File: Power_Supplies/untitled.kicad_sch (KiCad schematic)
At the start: 6 parts, among them U6 CS4391A-KZZ

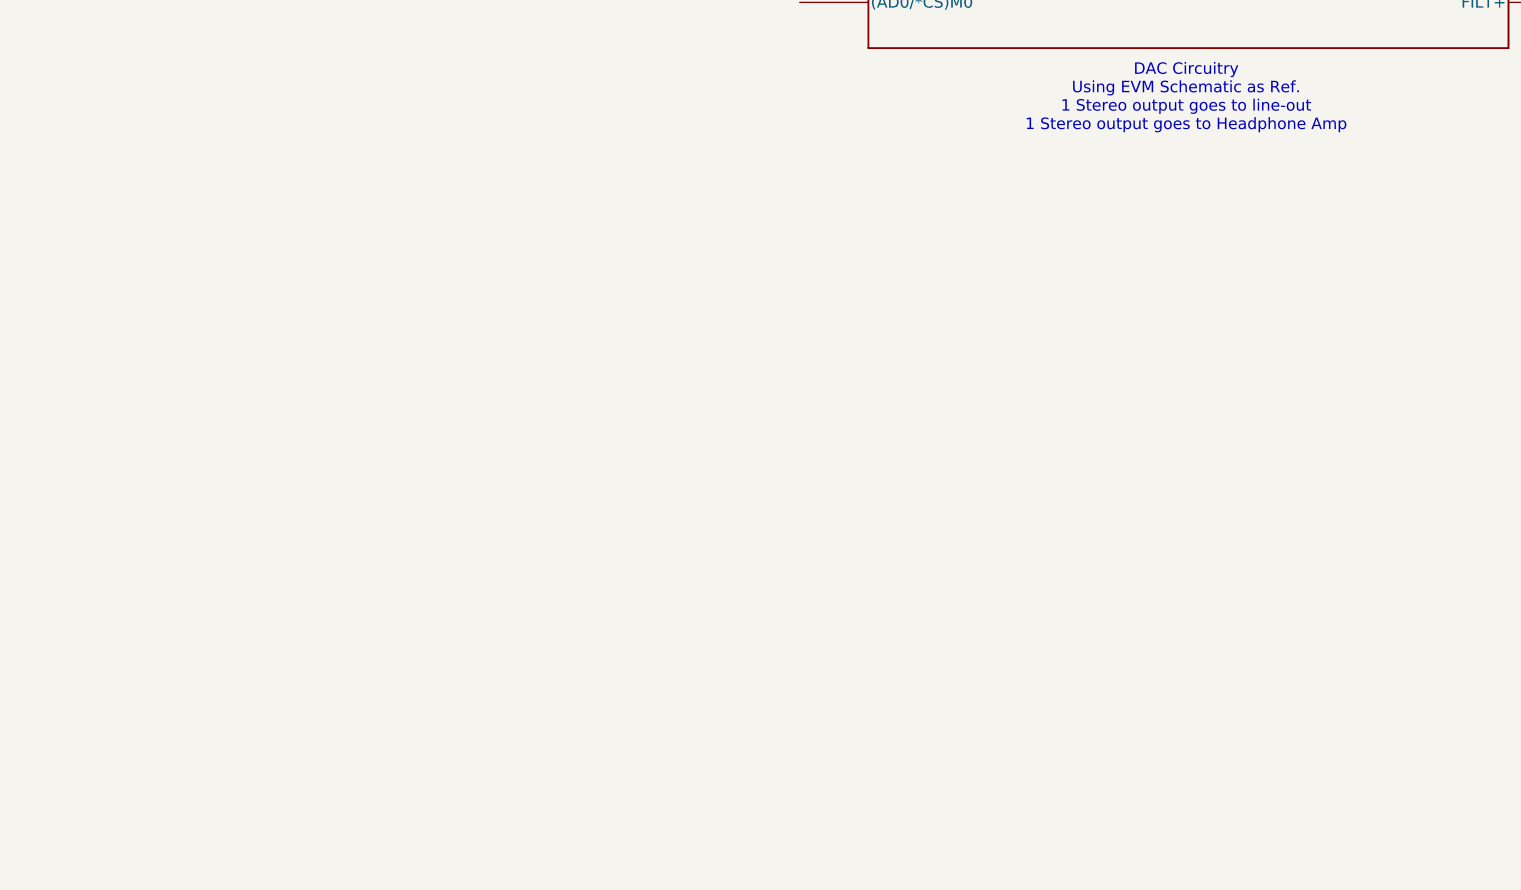
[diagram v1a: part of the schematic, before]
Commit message: Added Phantom Power, updated Xcore library things
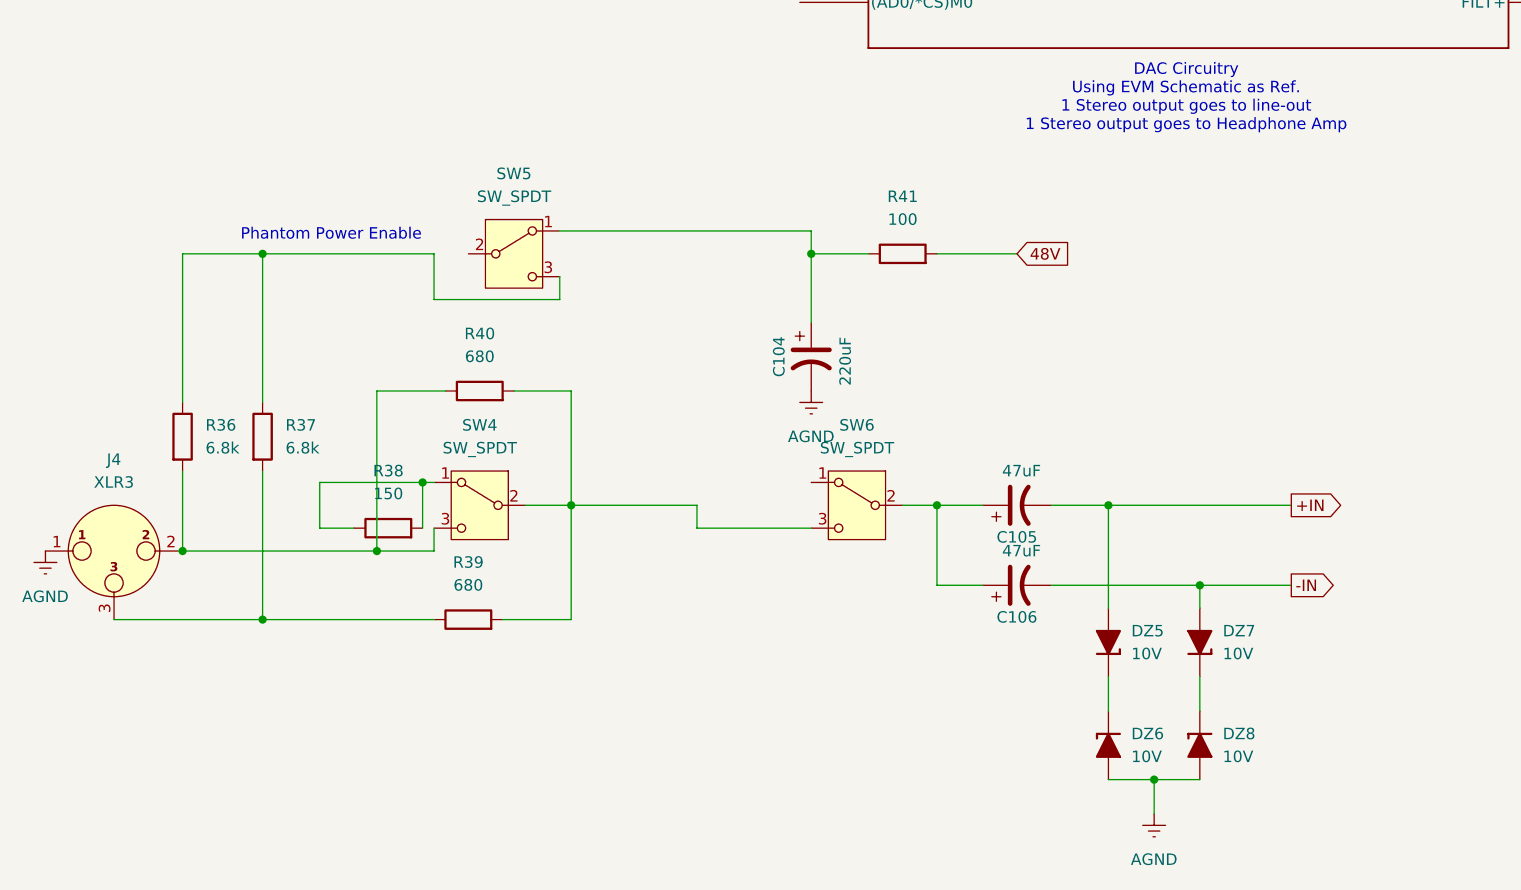
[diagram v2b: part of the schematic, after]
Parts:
- added C104: 220uF, Capacitor_SMD:CP_Elec_4x5.8, symbol Device:C_Polarized_US
- added C105, C106: 47uF, Capacitor_SMD:CP_Elec_4x5.8, symbol Device:C_Polarized_US
- added DZ5, DZ6, DZ7, DZ8: 10V, Diode_SMD:D_SMB, symbol PCM_Diode_Zener_AKL:D_Zener_Generic
- added J4: XLR3, symbol Connector_Audio:XLR3
- added R36, R37: 6.8k, Resistor_SMD:R_0805_2012Metric, symbol Device:R
- added R38: 150, Resistor_SMD:R_0805_2012Metric, symbol Device:R
- added R39, R40: 680, Resistor_SMD:R_0805_2012Metric, symbol Device:R
- added R41: 100, Resistor_SMD:R_0805_2012Metric, symbol Device:R
- added SW4, SW5, SW6: SW_SPDT, symbol Switch:SW_SPDT
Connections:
- net AGND: now also C104.2, DZ6.2 (A), DZ8.2 (A), J4.1
- new net: R38.1, R38.2, SW4.1 (A)
- new net: DZ5.1 (K), DZ6.1 (K)
- new net: C104.1, R41.1, SW5.1 (A)
- new net: R36.1, R37.1, SW5.3 (C)
- new net: J4.2, R36.2, R40.1, SW4.3 (C)
- new net: R39.2, R40.2, SW4.2 (B), SW6.3 (C)
- new net: DZ7.1 (K), DZ8.1 (K)
- new net: C105.1, C106.1, SW6.2 (B)
- new net: J4.3, R37.2, R39.1
- new net +IN: C105.2, DZ5.2 (A)
- new net -IN: C106.2, DZ7.2 (A)
- new net 48V: R41.2
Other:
- note added: "Phantom Power Enable"

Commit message: Add files via upload
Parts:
- C104, C105, C106, C14, C15, C16, C17, C18, DZ5, DZ6, DZ7, DZ8, J4, R36, R37, R38, R39, R40, R41, SW4, SW5, SW6, U6: now left out of the parts list
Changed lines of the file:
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@@
 		(unit 1)
 		(exclude_from_sim no)
-		(in_bom yes)
-		(on_board yes)
+		(in_bom no)
+		(on_board no)
 		(dnp no)
 		(fields_autoplaced yes)
@@
 		(unit 1)
 		(exclude_from_sim no)
-		(in_bom yes)
-		(on_board yes)
+		(in_bom no)
+		(on_board no)
 		(dnp no)
 		(fields_autoplaced yes)
@@
 		(unit 1)
 		(exclude_from_sim no)
-		(in_bom yes)
-		(on_board yes)
+		(in_bom no)
+		(on_board no)
 		(dnp no)
 		(fields_autoplaced yes)
@@
 		(unit 1)
 		(exclude_from_sim no)
-		(in_bom yes)
-		(on_board yes)
+		(in_bom no)
+		(on_board no)
 		(dnp no)
 		(property "Reference" "C104"
@@
 		(unit 1)
 		(exclude_from_sim no)
-		(in_bom yes)
-		(on_board yes)
+		(in_bom no)
+		(on_board no)
 		(dnp no)
 		(fields_autoplaced yes)
@@
 		(unit 1)
 		(exclude_from_sim no)
-		(in_bom yes)
-		(on_board yes)
+		(in_bom no)
+		(on_board no)
 		(dnp no)
 		(fields_autoplaced yes)
@@
 		(unit 1)
 		(exclude_from_sim no)
-		(in_bom yes)
-		(on_board yes)
+		(in_bom no)
+		(on_board no)
 		(dnp no)
 		(fields_autoplaced yes)
@@
 		(unit 1)
 		(exclude_from_sim no)
-		(in_bom yes)
-		(on_board yes)
+		(in_bom no)
+		(on_board no)
 		(dnp no)
 		(fields_autoplaced yes)
@@
 		(unit 1)
 		(exclude_from_sim no)
-		(in_bom yes)
-		(on_board yes)
+		(in_bom no)
+		(on_board no)
 		(dnp no)
 		(property "Reference" "C17"
@@
 		(unit 1)
 		(exclude_from_sim no)
-		(in_bom yes)
-		(on_board yes)
+		(in_bom no)
+		(on_board no)
 		(dnp no)
 		(fields_autoplaced yes)
@@
 		(unit 1)
 		(exclude_from_sim no)
-		(in_bom yes)
-		(on_board yes)
+		(in_bom no)
+		(on_board no)
 		(dnp no)
 		(fields_autoplaced yes)
@@
 		(unit 1)
 		(exclude_from_sim no)
-		(in_bom yes)
-		(on_board yes)
+		(in_bom no)
+		(on_board no)
 		(dnp no)
 		(fields_autoplaced yes)
@@
 		(unit 1)
 		(exclude_from_sim no)
-		(in_bom yes)
-		(on_board yes)
+		(in_bom no)
+		(on_board no)
 		(dnp no)
 		(fields_autoplaced yes)
@@
 		(unit 1)
 		(exclude_from_sim no)
-		(in_bom yes)
-		(on_board yes)
+		(in_bom no)
+		(on_board no)
 		(dnp no)
 		(property "Reference" "C106"
@@
 		(unit 1)
 		(exclude_from_sim no)
-		(in_bom yes)
-		(on_board yes)
+		(in_bom no)
+		(on_board no)
 		(dnp no)
 		(fields_autoplaced yes)
@@
 		(unit 1)
 		(exclude_from_sim no)
-		(in_bom yes)
-		(on_board yes)
+		(in_bom no)
+		(on_board no)
 		(dnp no)
 		(property "Reference" "C14"
@@
 		(unit 1)
 		(exclude_from_sim no)
-		(in_bom yes)
-		(on_board yes)
+		(in_bom no)
+		(on_board no)
 		(dnp no)
 		(property "Reference" "C18"
@@
 		(unit 1)
 		(exclude_from_sim no)
-		(in_bom yes)
-		(on_board yes)
+		(in_bom no)
+		(on_board no)
 		(dnp no)
 		(property "Reference" "C16"
@@
 		(unit 1)
 		(exclude_from_sim no)
-		(in_bom yes)
-		(on_board yes)
+		(in_bom no)
+		(on_board no)
 		(dnp no)
 		(property "Reference" "SW4"
@@
 		(unit 1)
 		(exclude_from_sim no)
-		(in_bom yes)
-		(on_board yes)
+		(in_bom no)
+		(on_board no)
 		(dnp no)
 		(property "Reference" "C15"
@@
 		(unit 1)
 		(exclude_from_sim no)
-		(in_bom yes)
-		(on_board yes)
+		(in_bom no)
+		(on_board no)
 		(dnp no)
 		(fields_autoplaced yes)
@@
 		(unit 1)
 		(exclude_from_sim no)
-		(in_bom yes)
-		(on_board yes)
+		(in_bom no)
+		(on_board no)
 		(dnp no)
 		(fields_autoplaced yes)
@@
 		(unit 1)
 		(exclude_from_sim no)
-		(in_bom yes)
-		(on_board yes)
+		(in_bom no)
+		(on_board no)
 		(dnp no)
 		(property "Reference" "C105"
@@
 		(unit 1)
 		(exclude_from_sim no)
-		(in_bom yes)
-		(on_board yes)
+		(in_bom no)
+		(on_board no)
 		(dnp no)
 		(fields_autoplaced yes)
@@
 		(unit 1)
 		(exclude_from_sim no)
-		(in_bom yes)
-		(on_board yes)
+		(in_bom no)
+		(on_board no)
 		(dnp no)
 		(fields_autoplaced yes)
@@
 		(unit 1)
 		(exclude_from_sim no)
-		(in_bom yes)
-		(on_board yes)
+		(in_bom no)
+		(on_board no)
 		(dnp no)
 		(fields_autoplaced yes)
@@
 		(unit 1)
 		(exclude_from_sim no)
-		(in_bom yes)
-		(on_board yes)
+		(in_bom no)
+		(on_board no)
 		(dnp no)
 		(property "Reference" "SW6"
@@
 		(unit 1)
 		(exclude_from_sim no)
-		(in_bom yes)
-		(on_board yes)
+		(in_bom no)
+		(on_board no)
 		(dnp no)
 		(fields_autoplaced yes)

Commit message: Add files via upload
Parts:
- added C137, C33, C44, C46, C47: 10uF, Capacitor_SMD:CP_Elec_4x5.8, symbol Device:C_Polarized_US
- added C42, C43, C45: 0.1uF, Capacitor_SMD:C_0805_2012Metric, symbol Device:C
- added C48, C49: 1uF, Capacitor_SMD:CP_Elec_4x5.8, symbol Device:C_Polarized_US
- added IC2: PCM1808PWRG4, SamacSys_Parts:SOP65P640X120-14N, symbol SamacSys_Parts:PCM1808PWRG4
- added U9: MAX1044, SamacSys_Parts:SOIC127P600X175-8N, symbol Regulator_SwitchedCapacitor:MAX1044
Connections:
- net AGND: now also C137.1, C42.2, C43.1, C44.2, C45.2, C46.2, C47.2, IC2.2 (AGND), IC2.5 (DGND), U9.3 (GND), U9.6 (LV)
- new net: C44.1, C45.1, IC2.1 (VREF)
- new net: C49.1, IC2.13 (VINL)
- new net: C48.1, IC2.14 (VINR)
- new net: C33.1, U9.2 (CAP+)
- new net: C33.2, U9.4 (CAP-)
- new net -5V: C137.2, U9.5 (VOUT)
- new net 3.3V: C43.2, C47.1, IC2.4 (VDD)
- new net 5V: C42.1, C46.1, IC2.3 (VCC), U9.8 (V+)
- new net A_L_5: C49.2
- new net A_R_5: C48.2
- new net DATA_BIT_CLOCK: IC2.8 (BCK)
- new net D_OUT_1: IC2.9 (DOUT)
- new net FORMAT_SELECT: IC2.12 (FMT)
- new net LRCK: IC2.7 (LRCK)
- new net MCLK: IC2.6 (SCKI)
- new net MODE_0: IC2.10 (MD0)
- new net MODE_1: IC2.11 (MD1)
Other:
- note added: "OLD ADC"
- note added: "OLD DAC"
- note added: "OLD PHANTOM POWER CIRCUIT"
- note added: "Old voltage inverter (needed more current output)"

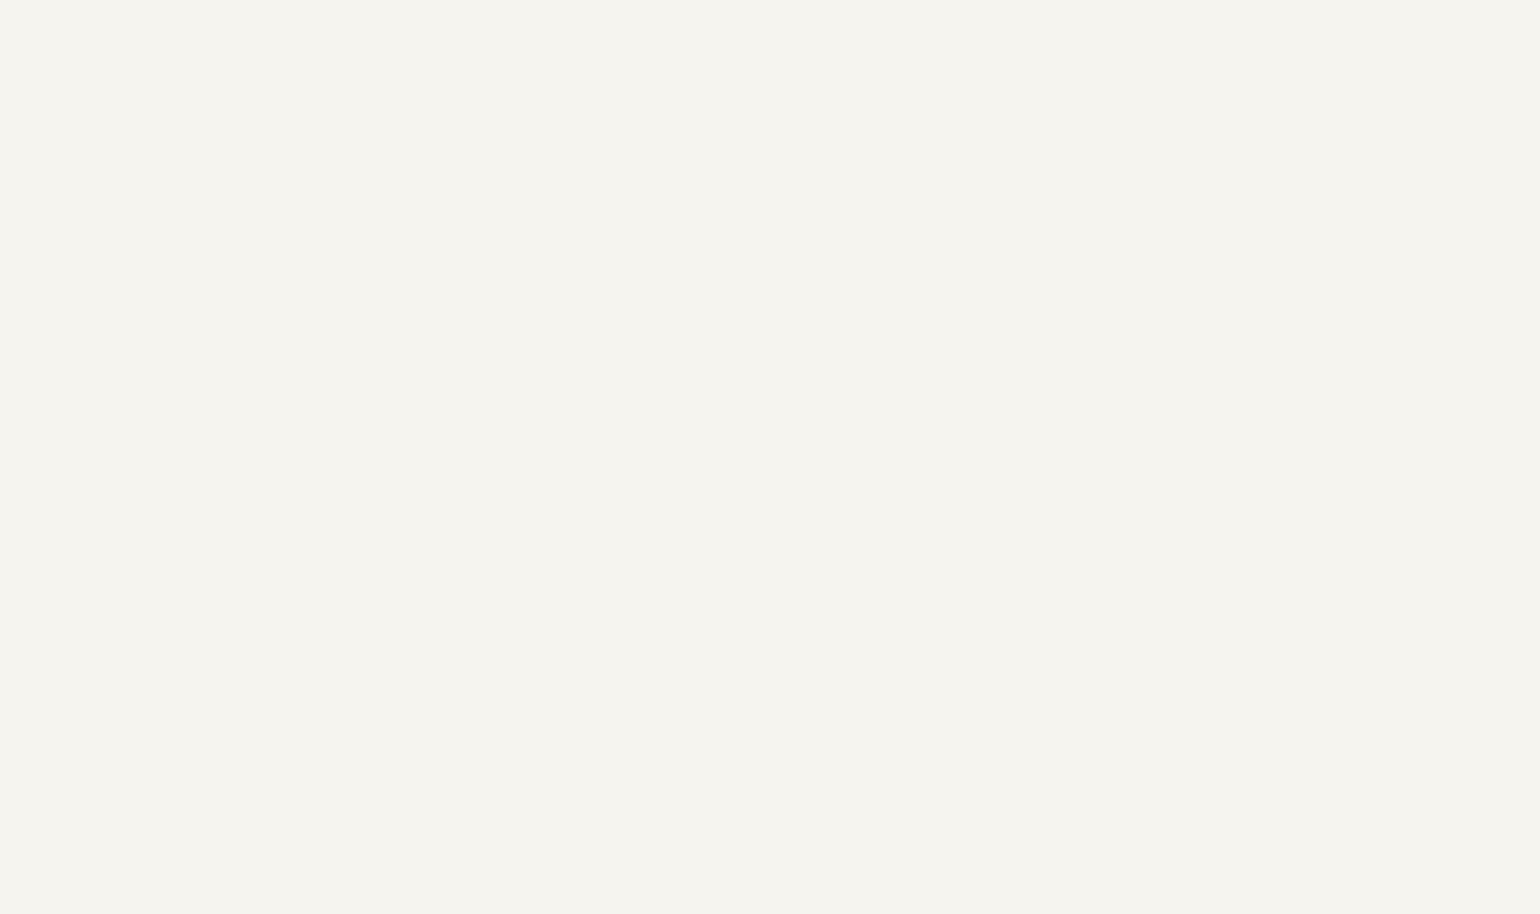
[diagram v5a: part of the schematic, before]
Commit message: New preamp design + some added files
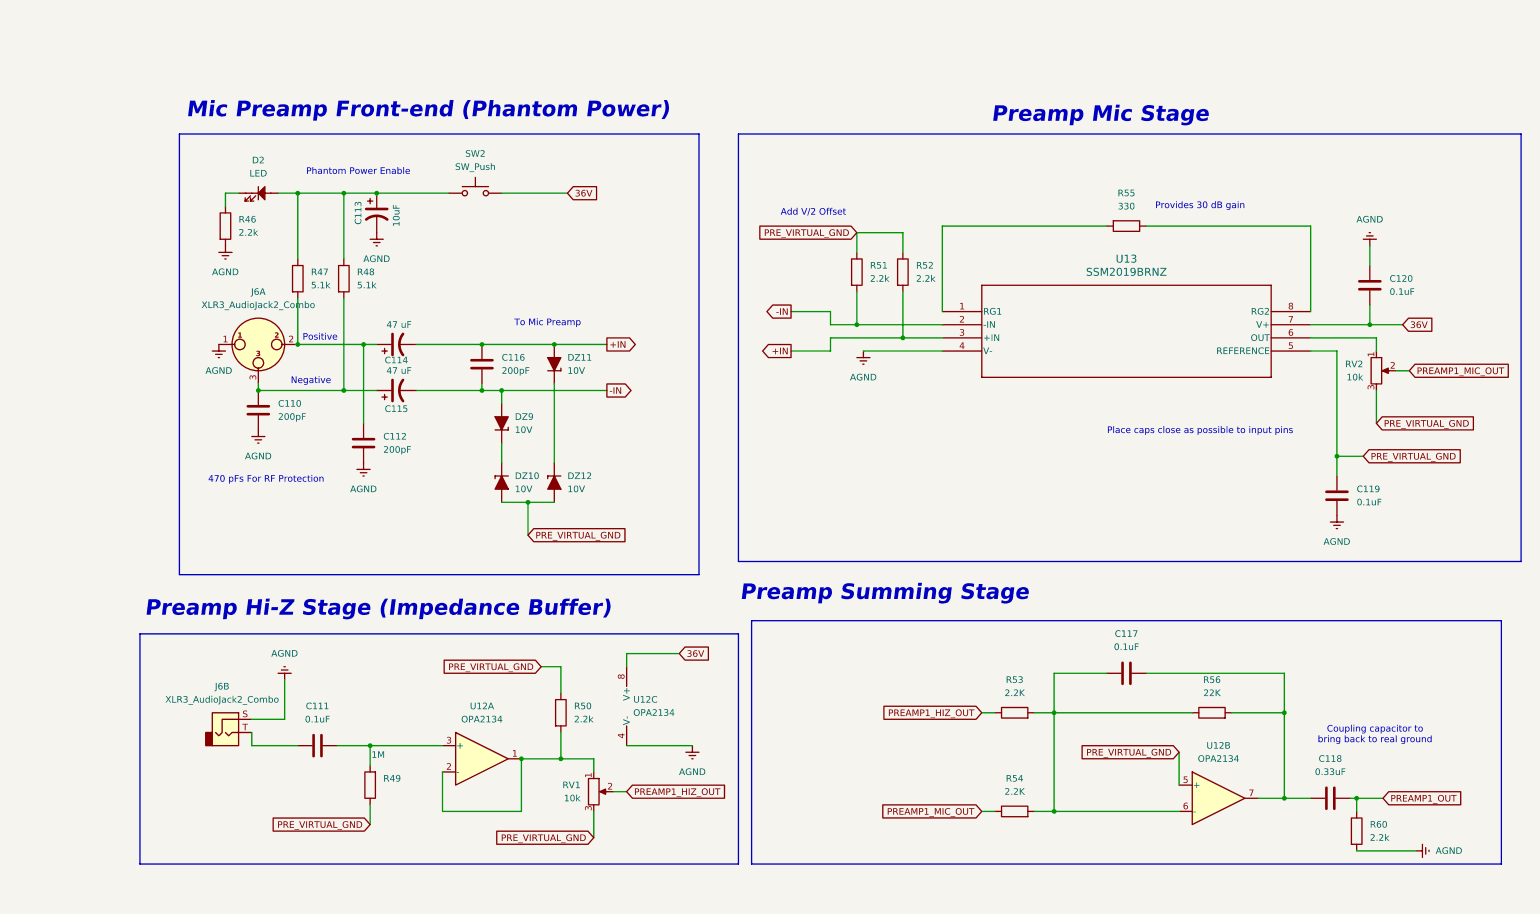
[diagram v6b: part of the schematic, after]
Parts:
- added C110, C112, C116: 200pF, Capacitor_SMD:C_0402_1005Metric, symbol Device:C
- added C111, C117, C119, C120: 0.1uF, Capacitor_SMD:C_0402_1005Metric, symbol Device:C
- added C113: 10uF, Capacitor_SMD:CP_Elec_4x5.8, symbol Device:C_Polarized_US
- added C114, C115: 47 uF, Capacitor_SMD:CP_Elec_4x5.8, symbol Device:C_Polarized_US
- added C118: 0.33uF, Capacitor_SMD:C_0402_1005Metric, symbol Device:C
- added D2: LED, LED_SMD:LED_0201_0603Metric, symbol PCM_SL_Devices:LED
- added DZ10, DZ11, DZ12, DZ9: 10V, Diode_SMD:D_SMB, symbol PCM_Diode_Zener_AKL:D_Zener_Generic
- added J6: XLR3_AudioJack2_Combo, SamacSys_Parts:FA-238_EPS, symbol Connector_Audio:XLR3_AudioJack2_Combo
- added R46, R50, R51, R52, R60: 2.2k, Resistor_SMD:R_0805_2012Metric, symbol Device:R
- added R47, R48: 5.1k, Resistor_SMD:R_0805_2012Metric, symbol Device:R
- added R49: 1M, Resistor_SMD:R_0805_2012Metric, symbol Device:R
- added R53, R54: 2.2K, Resistor_SMD:R_0805_2012Metric, symbol Device:R
- added R55: 330, Resistor_SMD:R_0805_2012Metric, symbol Device:R
- added R56: 22K, Resistor_SMD:R_0805_2012Metric, symbol Device:R
- added RV1, RV2: 10k, Potentiometer_THT:Potentiometer_ACP_CA9-V10_Vertical, symbol Device:R_Potentiometer
- added SW2: SW_Push, Button_Switch_THT:SW_PUSH_1P1T_6x3.5mm_H5.0_APEM_MJTP1250, symbol Switch:SW_Push
- added U12: OPA2134, Package_SO:SOIC-8_3.9x4.9mm_P1.27mm, symbol Amplifier_Operational:OPA2134
- added U13: SSM2019BRNZ, SamacSys_Parts:SOIC127P600X175-8N, symbol SDLibrary:SSM2019BRNZ
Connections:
- net +IN: now also C114.2, C116.2, DZ11.2 (A), R52.2, U13.3 (+IN)
- net -IN: now also C115.2, C116.1, DZ9.2 (A), R51.2, U13.2 (-IN)
- net AGND: now also C110.1, C112.1, C113.2, C119.2, C120.2, J6.1, J6.S, R46.2, R60.2, U12.4 (V-), U13.4 (V-)
- new net: C117.2, R53.2, R54.2, R56.1, U12.6 (-)
- new net: C117.1, C118.2, R56.2, U12.7
- new net: R55.1, U13.8 (RG2)
- new net: R55.2, U13.1 (RG1)
- new net: D2.1, R46.1
- new net: C111.1, R49.2, U12.3 (+)
- new net: DZ11.1 (K), DZ12.1 (K)
- new net: DZ10.1 (K), DZ9.1 (K)
- new net: RV2.1, U13.6 (OUT)
- new net: C110.2, C115.1, J6.3, R48.2
- new net: C112.2, C114.1, J6.2, R47.2
- new net: C113.1, D2.2, R47.1, R48.1, SW2.1
- new net: R50.2, RV1.1, U12.1, U12.2 (-)
- new net: C111.2, J6.T
- new net 36V: C120.1, SW2.2, U12.8 (V+), U13.7 (V+)
- new net PREAMP1_HIZ_OUT: R53.1, RV1.2
- new net PREAMP1_MIC_OUT: R54.1, RV2.2
- new net PREAMP1_OUT: C118.1, R60.1
- new net PRE_VIRTUAL_GND: C119.1, DZ10.2 (A), DZ12.2 (A), R49.1, R50.1, R51.1, R52.1, RV1.3, RV2.3, U12.5 (+), U13.5 (REFERENCE)
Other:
- note added: "470 pFs For RF Protection"
- note added: "Add V/2 Offset"
- note added: "Coupling capacitor to bring back to real ground"
- note added: "Mic Preamp Front-end (Phantom Power)"
- note added: "Negative"
- note added: "Place caps close as possible to input pins"
- note added: "Positive"
- note added: "Preamp Hi-Z Stage (Impedance Buffer)"
- note added: "Preamp Mic Stage"
- note added: "Preamp Summing Stage"
- note added: "Provides 30 dB gain"
- note added: "To Mic Preamp"

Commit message: Finished HiZ Inputs
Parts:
- added C102, C107: 22uF, Capacitor_SMD:CP_Elec_4x5.8, symbol Device:C_Polarized_US
- added C32: 10uF, Capacitor_SMD:CP_Elec_4x5.8, symbol Device:C_Polarized_US
- added D1: LED, LED_SMD:LED_0201_0603Metric, symbol PCM_SL_Devices:LED
- added DZ1, DZ2, DZ3, DZ4: 10V, Diode_SMD:D_SMB, symbol PCM_Diode_Zener_AKL:D_Zener_Generic
- added J8: XLR3, symbol Connector_Audio:XLR3
- added R30: 2.2k, Resistor_SMD:R_0805_2012Metric, symbol Device:R
- added R31, R32: 5.1k, Resistor_SMD:R_0805_2012Metric, symbol Device:R
- added R33, R45: 10, Resistor_SMD:R_0805_2012Metric, symbol Device:R
- added SW1: SW_Push, Button_Switch_THT:SW_PUSH_1P1T_6x3.5mm_H5.0_APEM_MJTP1250, symbol Switch:SW_Push
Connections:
- net +IN: now also DZ3.2 (A), R33.2
- net -IN: now also DZ1.2 (A), R45.2
- net 36V: now also SW1.2
- net AGND: now also C32.2, DZ2.2 (A), DZ4.2 (A), J8.1, R30.2
- new net: C32.1, D1.2, R31.1, R32.1, SW1.1
- new net: C107.1, J8.3, R32.2
- new net: C107.2, R45.1
- new net: DZ3.1 (K), DZ4.1 (K)
- new net: DZ1.1 (K), DZ2.1 (K)
- new net: C102.1, J8.2, R31.2
- new net: D1.1, R30.1
- new net: C102.2, R33.1
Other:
- note added: "Phantom Power Circuit"
